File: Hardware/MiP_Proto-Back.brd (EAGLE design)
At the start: 69.9 x 61.3 mm, 9 parts

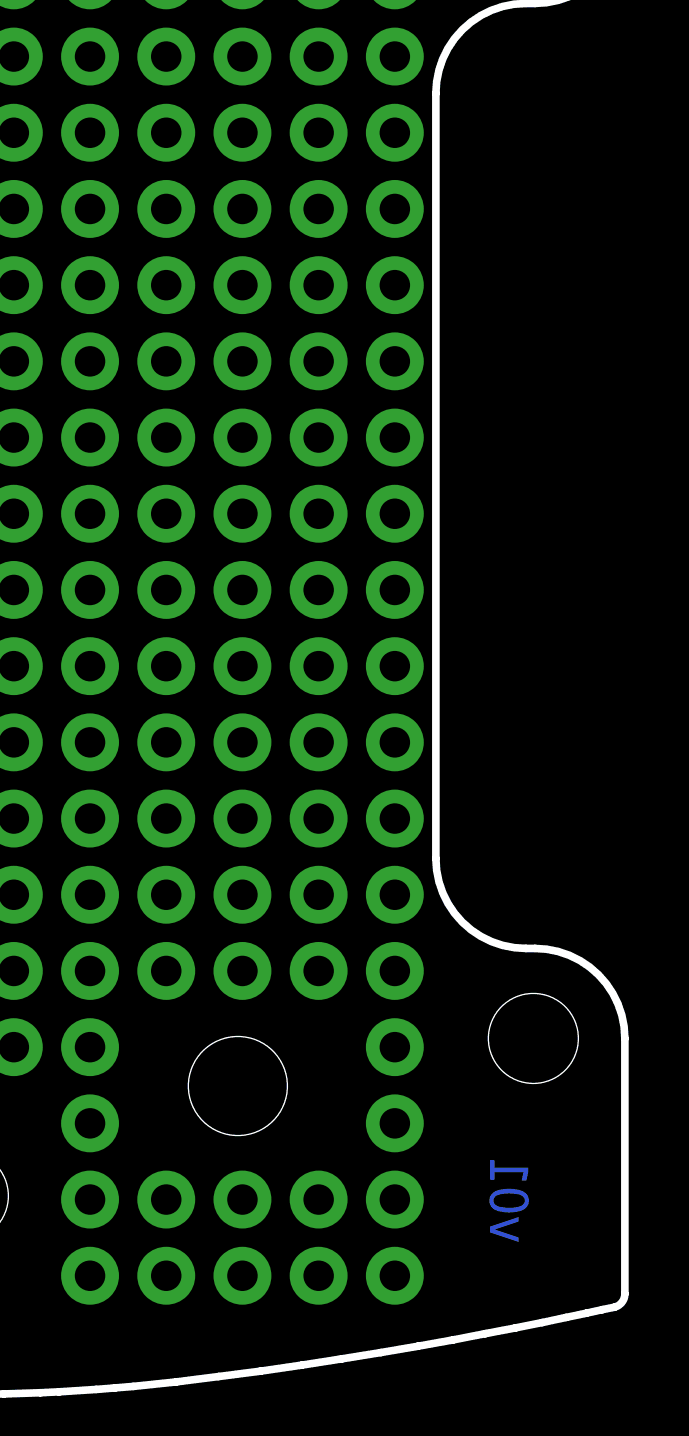
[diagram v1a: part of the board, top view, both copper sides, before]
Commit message: changed rev numbers, added name to PCB.
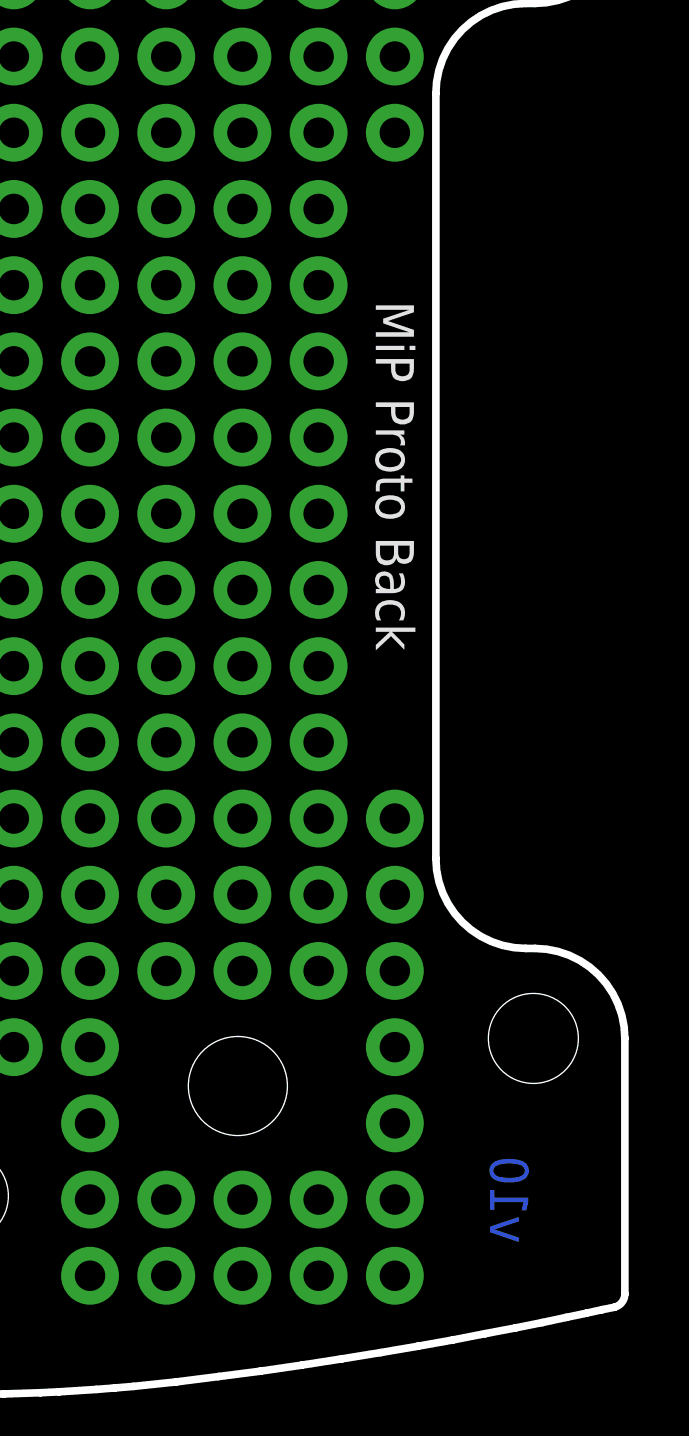
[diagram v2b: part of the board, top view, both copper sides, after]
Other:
- board text added: "MiP Proto Back"
- board text added: "v10"
- board text removed: "v01"
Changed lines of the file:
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@@
 <hole x="66.8476" y="-18.7594" drill="3"/>
 <wire x1="-1.6524" y1="-0.0094" x2="79.3476" y2="-0.0094" width="0.282" layer="48"/>
-<text x="40.64" y="-39.37" size="1.778" layer="51" ratio="15">Casey Kuhns</text>
+<text x="44.45" y="-39.37" size="1.778" layer="51" ratio="15">Casey Kuhns</text>
 <text x="36.83" y="21.082" size="0.8128" layer="21" font="vector" ratio="15" rot="R180" align="center">GND</text>
 <text x="39.37" y="21.082" size="0.8128" layer="21" font="vector" ratio="15" rot="R180" align="center">RX</text>
@@
 <text x="41.91" y="21.082" size="0.8128" layer="22" font="vector" ratio="15" rot="MR180" align="center">TX</text>
 <text x="44.45" y="21.082" size="0.8128" layer="22" font="vector" ratio="15" rot="MR180" align="center">6V</text>
-<text x="66.04" y="-24.13" size="1.27" layer="16" font="vector" ratio="15" rot="MR270" align="center">v01</text>
+<text x="66.04" y="-24.13" size="1.27" layer="16" font="vector" ratio="15" rot="MR270" align="center">v10</text>
+<text x="62.23" y="0" size="1.27" layer="21" font="vector" ratio="15" rot="SR270" align="center">MiP Proto Back</text>
+<text x="62.23" y="0" size="1.27" layer="22" font="vector" ratio="15" rot="SMR90" align="center">MiP Proto Back</text>
 </plain>
 <attributes>
@@
 <via x="59.69" y="-8.89" extent="1-16" drill="1.016" diameter="1.9304"/>
 </signal>
-<signal name="N$183">
-<via x="62.23" y="-8.89" extent="1-16" drill="1.016" diameter="1.9304"/>
-</signal>
 <signal name="N$184">
 <via x="54.61" y="-6.35" extent="1-16" drill="1.016" diameter="1.9304"/>
@@
 <via x="59.69" y="-6.35" extent="1-16" drill="1.016" diameter="1.9304"/>
 </signal>
-<signal name="N$187">
-<via x="62.23" y="-6.35" extent="1-16" drill="1.016" diameter="1.9304"/>
-</signal>
 <signal name="N$188">
 <via x="54.61" y="-3.81" extent="1-16" drill="1.016" diameter="1.9304"/>
@@
 <via x="59.69" y="-3.81" extent="1-16" drill="1.016" diameter="1.9304"/>
 </signal>
-<signal name="N$191">
-<via x="62.23" y="-3.81" extent="1-16" drill="1.016" diameter="1.9304"/>
-</signal>
 <signal name="N$192">
 <via x="54.61" y="-1.27" extent="1-16" drill="1.016" diameter="1.9304"/>
@@
 <via x="59.69" y="-1.27" extent="1-16" drill="1.016" diameter="1.9304"/>
 </signal>
-<signal name="N$195">
-<via x="62.23" y="-1.27" extent="1-16" drill="1.016" diameter="1.9304"/>
-</signal>
 <signal name="N$196">
 <via x="44.45" y="8.89" extent="1-16" drill="1.016" diameter="1.9304"/>
@@
 <via x="59.69" y="1.27" extent="1-16" drill="1.016" diameter="1.9304"/>
 </signal>
-<signal name="N$224">
-<via x="62.23" y="8.89" extent="1-16" drill="1.016" diameter="1.9304"/>
-</signal>
-<signal name="N$225">
-<via x="62.23" y="6.35" extent="1-16" drill="1.016" diameter="1.9304"/>
-</signal>
-<signal name="N$226">
-<via x="62.23" y="3.81" extent="1-16" drill="1.016" diameter="1.9304"/>
-</signal>
-<signal name="N$227">
-<via x="62.23" y="1.27" extent="1-16" drill="1.016" diameter="1.9304"/>
-</signal>
 <signal name="N$228">
